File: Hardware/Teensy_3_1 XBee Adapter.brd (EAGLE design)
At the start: 27.9 x 86.4 mm, 34 parts

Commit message: Opened the board up a bit
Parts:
- removed EXT_PWR: M02PTH, SparkFun-Connectors:1X02
- added EXT_3.3V: M02PTH, SparkFun-Connectors:1X02
- JP1: value TEENSY-3.1 -> TEENSY-3.1NOSILK; device Testing:TEENSY-3.1 -> Testing:TEENSY-3.1_NOSILK
- LOGO2: value OSHW-LOGOS -> OSHW-LOGOM; device SparkFun-Aesthetics:OSHW-LOGO-S -> SparkFun-Aesthetics:OSHW-LOGO-M
- LOGO3: value SFE_LOGO_NAME_FLAME.1_INCH -> SFE_LOGO_NAME_FLAME.2_INCH; device SparkFun-Aesthetics:SFE_LOGO_NAME_FLAME_.1 -> SparkFun-Aesthetics:SFE_LOGO_NAME_FLAME_.2
- moved SJ1 53.3 mm to (5.08, 53.3)
- moved S2 49.9 mm to (10.2, 52.1)
- moved SJ3 48.4 mm to (5.08, 50.8)
- moved STANDOFF1 30.7 mm to (27.9, 81.3)
- moved STANDOFF2 30.5 mm to (5.08, 81.3)
- moved LED1 28.3 mm to (27.3, 54.6), turned to 270 degrees
- moved FID2 25.4 mm to (31.8, 1.27)
- moved FID1 24.1 mm to (1.27, 85.1)
- moved R11 24.1 mm to (24.1, 54.6), turned to 180 degrees
- moved LOGO2 16.6 mm to (21.6, 3.49)
- moved FRAME1 11.4 mm to (-17.8, -11.4)
- moved R1 10.9 mm to (15.2, 74.9)
- moved R3 10.9 mm to (12.7, 74.9)
- moved LOGO3 10.2 mm to (12.4, 14.6)
- moved STANDOFF3 9.25 mm to (16.5, 2.54)
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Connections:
- removed net EXT_PWR: EXT_PWR.2, SJ4.1, SJ5.2
- new net EXT_3.3V: EXT_3.3V.2, SJ4.1, SJ5.2
- net GND: now also EXT_3.3V.1; no longer EXT_PWR.1
- net IN: now also S2.5; no longer S2.2
- net N$140: now also S2.6; no longer S2.3
- net N$141: now also S2.3; no longer S2.6
- net OUT: now also S2.2; no longer S2.5
- net UART_RX: now also S2.1; no longer S2.4
- net UART_TX: now also S2.4; no longer S2.1
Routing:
- net EXT_3.3V: track 0.00 -> 71.8 mm, vias 0 -> 2
- net IN: track 112.8 -> 49.3 mm, vias 1 -> 2
- net EXT_PWR: track 52.3 -> 0.00 mm
- net OUT: track 101.9 -> 50.0 mm, vias 1 -> 3
- net UART_RX: track 11.7 -> 62.7 mm, vias 1 -> 2
- net UART_TX: track 21.0 -> 62.9 mm, vias 1 -> 2
- net N$43: track 17.3 -> 8.22 mm, vias 2 -> 0
- net XBEE_VDD: track 66.2 -> 57.4 mm
- net N$17: track 2.08 -> 9.50 mm
- net GND: track 56.9 -> 49.5 mm, vias 20 -> 25
- net N$19: track 2.08 -> 9.35 mm
- net A7/21: track 39.3 -> 44.1 mm
- net A5/19/SCL0: track 5.39 -> 9.72 mm
- net A9/23: track 5.39 -> 9.72 mm
- net A4/18/SDA0: track 5.39 -> 9.72 mm
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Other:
- board size 27.9 x 86.4 mm -> 33 x 86.4 mm
- board text added: "-"
- board text added: "0/RX1"
- board text added: "1/TX1"
- board text added: "11"
- board text added: "12"
- board text added: "13"
- board text added: "2"
- board text added: "3.3V"
- board text added: "3V"
- board text added: "7/RX3"
- board text added: "8/TX3"
- board text added: "A0/14"
- board text added: "A1/15"
- board text added: "A10"
- board text added: "A11"
- board text added: "A14/DAC"
- board text added: "A2/16"
- board text added: "A3/17"
- board text added: "A4/18"
- board text added: "A5/19"
- board text added: "A6/20"
- board text added: "A7/21"
- board text added: "A8/22"
- board text added: "A9/23"
- board text added: "AGND"
- board text added: "AREF"
- board text added: "DGND"
- board text added: "EXT"
- board text added: "EXT_PWR"
- board text added: "Pgm"
- board text added: "TNSY"
- board text added: "Teensy 3.1"
- board text added: "UART1"
- board text added: "VBat"
- board text added: "VIN"
- board text added: "VUSB"
- board text added: "Vin"
- board text added: "XBee"
- board text added: "~10/.."
- board text added: "~3"
- board text added: "~4"
- board text added: "~5"
- board text added: "~6"
- board text added: "~9/.."
- board text removed: "D3/D2"
- board text removed: "TNSY_PWR"
- board text removed: "UART"
- board text removed: "XBEE"

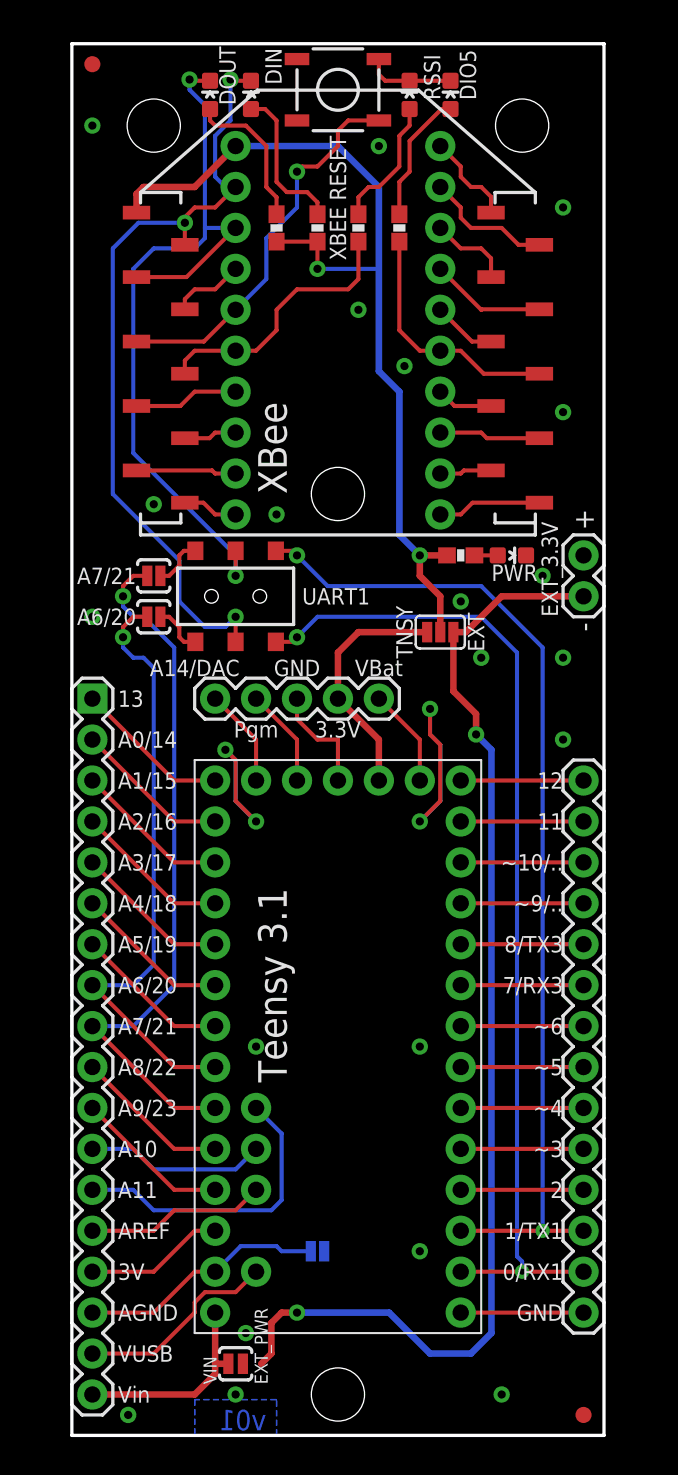
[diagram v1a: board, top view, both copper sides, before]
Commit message: Fixed silk.  Preparing for first proto
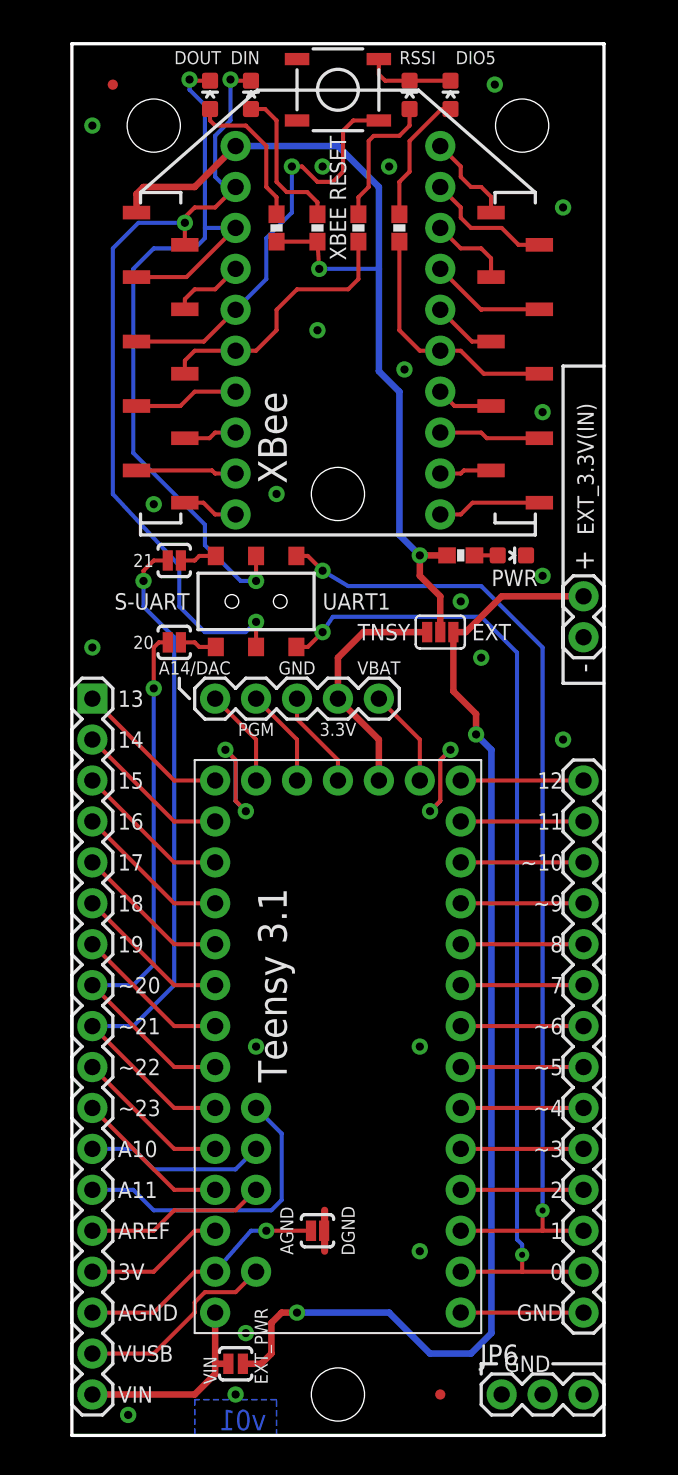
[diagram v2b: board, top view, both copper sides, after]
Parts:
- removed EXT_3.3V: M02PTH, SparkFun-Connectors:1X02
- added EXT_3.3V(IN): M02PTH, SparkFun-Connectors:1X02
- added JP6: (no value), SparkFun-Connectors:1X03
- FID1, FID2: value FIDUCIAL1X2 -> FIDUCIALUFIDUCIAL; device SparkFun-Aesthetics:FIDUCIAL-1X2 -> SparkFun-Aesthetics:MICRO-FIDUCIAL
- SJ2: device SparkFun:SJ_2S -> SparkFun-Passives:PAD-JUMPER-2-NC_BY_PASTE_YES_SILK
- moved FID2 8.98 mm to (22.9, 2.54)
- moved SJ3 2.03 mm to (6.35, 49.2)
- moved FID1 1.80 mm to (2.54, 83.8)
- moved SJ1 1.59 mm to (6.35, 54.3)
- moved S2 1.31 mm to (11.4, 51.8)
- moved SJ2 1.27 mm to (15.2, 12.7), flipped to the top, turned to 0 degrees
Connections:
- net EXT_3.3V: now also EXT_3.3V(IN).2; no longer EXT_3.3V.2
- net GND: now also EXT_3.3V(IN).1, JP6.1, JP6.2, JP6.3; no longer EXT_3.3V.1
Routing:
- net GND: track 49.5 -> 42.6 mm
- net A6/20: track 37.9 -> 34.7 mm
- net RESET: track 24.1 -> 26.2 mm
- net UART_TX: track 62.9 -> 61.3 mm
- net OUT: track 50.0 -> 51.5 mm
- net IN: track 49.3 -> 50.7 mm
- net EXT_3.3V: track 71.8 -> 72.9 mm
- net UART_RX: track 62.7 -> 61.7 mm
- net N$141: track 3.18 -> 2.29 mm
- net N$140: track 3.18 -> 2.29 mm
- net N$43: track 8.22 -> 8.77 mm
- net AGND: track 15.4 -> 15.8 mm, vias 0 -> 1
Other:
- board text added: "0"
- board text added: "1"
- board text added: "14"
- board text added: "15"
- board text added: "16"
- board text added: "17"
- board text added: "18"
- board text added: "19"
- board text added: "20"
- board text added: "21"
- board text added: "7"
- board text added: "8"
- board text added: "PGM"
- board text added: "S-UART"
- board text added: "VBAT"
- board text added: "~10"
- board text added: "~20"
- board text added: "~21"
- board text added: "~22"
- board text added: "~23"
- board text added: "~9"
- board text removed: "0/RX1"
- board text removed: "1/TX1"
- board text removed: "7/RX3"
- board text removed: "8/TX3"
- board text removed: "A0/14"
- board text removed: "A1/15"
- board text removed: "A2/16"
- board text removed: "A3/17"
- board text removed: "A4/18"
- board text removed: "A5/19"
- board text removed: "A6/20"
- board text removed: "A7/21"
- board text removed: "A8/22"
- board text removed: "A9/23"
- board text removed: "Pgm"
- board text removed: "VBat"
- board text removed: "Vin"
- board text removed: "~10/.."
- board text removed: "~9/.."

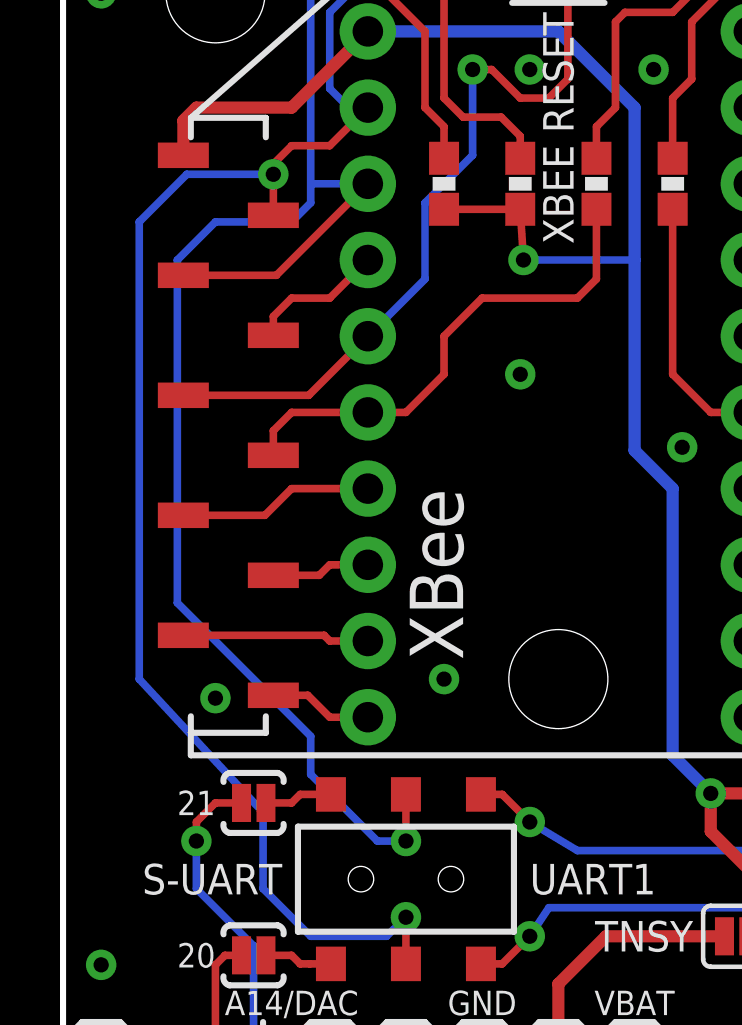
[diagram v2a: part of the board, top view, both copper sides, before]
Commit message: Fliping bottom silk labels
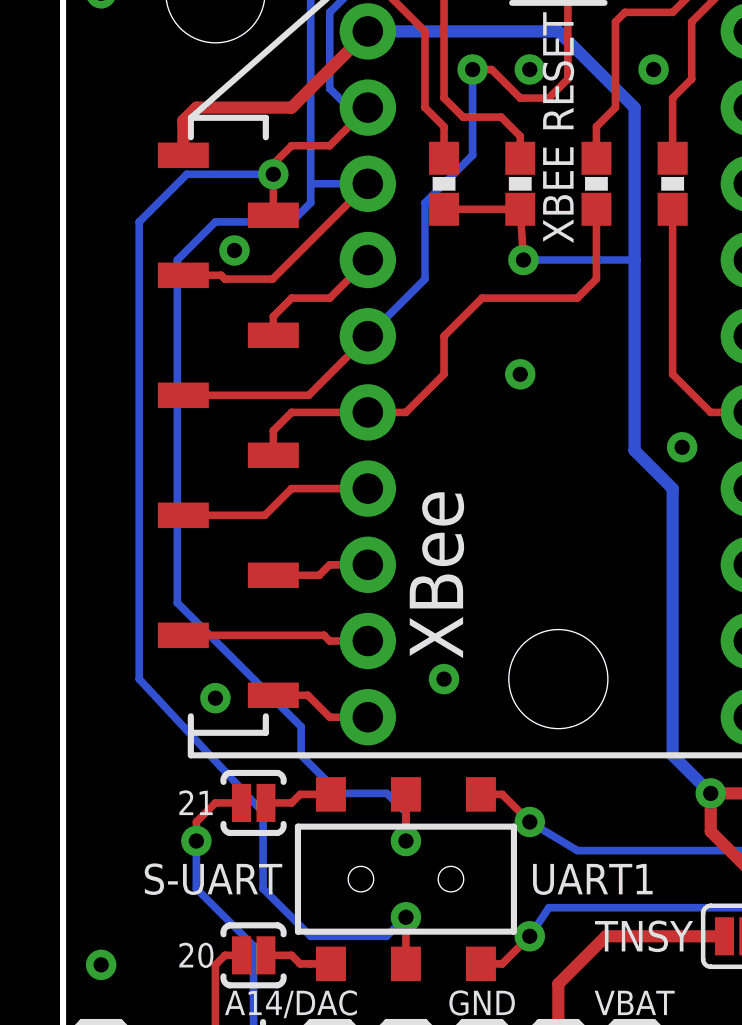
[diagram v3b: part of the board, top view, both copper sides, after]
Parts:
- moved LOGO2 0.71 mm to (22.2, 3.17), turned to 0 degrees
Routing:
- net GND: vias 25 -> 26
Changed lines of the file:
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@@
 <grid distance="0.1" unitdist="inch" unit="inch" style="lines" multiple="1" display="yes" altdistance="0.0125" altunitdist="inch" altunit="inch"/>
 <layers>
-<layer number="1" name="Top" color="4" fill="1" visible="yes" active="yes"/>
+<layer number="1" name="Top" color="4" fill="1" visible="no" active="yes"/>
 <layer number="2" name="Route2" color="1" fill="3" visible="no" active="no"/>
 <layer number="3" name="Route3" color="4" fill="3" visible="no" active="no"/>
@@
 <text x="11.43" y="64.77" size="1.016" layer="22" font="vector" ratio="15" rot="MR0" align="center-right">DIO11</text>
 <text x="11.43" y="62.23" size="1.016" layer="22" font="vector" ratio="15" rot="MR0" align="center-right">RES</text>
-<text x="11.43" y="59.69" size="1.016" layer="22" font="vector" ratio="15" rot="MR0" align="center-right">DTR</text>
-<text x="11.43" y="57.15" size="1.016" layer="22" font="vector" ratio="15" rot="MR0" align="center-right">GND</text>
+<text x="8.5725" y="59.69" size="1.016" layer="22" font="vector" ratio="15" rot="MR0" align="center-left">DTR</text>
+<text x="8.5725" y="57.15" size="1.016" layer="22" font="vector" ratio="15" rot="MR0" align="center-left">GND</text>
 <text x="21.2471" y="77.47" size="1.016" layer="22" font="vector" ratio="15" rot="MR0" align="center-left">DIO1</text>
 <text x="21.2471" y="74.93" size="1.016" layer="22" font="vector" ratio="15" rot="MR0" align="center-left">DIO2</text>
 <text x="21.2471" y="72.39" size="1.016" layer="22" font="vector" ratio="15" rot="MR0" align="center-left">DIO3</text>
-<text x="24.4221" y="69.85" size="1.016" layer="22" font="vector" ratio="15" rot="MR0" align="center-right">RTS</text>
-<text x="24.4221" y="67.31" size="1.016" layer="22" font="vector" ratio="15" rot="MR0" align="center-right">DIO5</text>
-<text x="24.4221" y="64.77" size="1.016" layer="22" font="vector" ratio="15" rot="MR0" align="center-right">RES</text>
-<text x="24.4221" y="62.23" size="1.016" layer="22" font="vector" ratio="15" rot="MR0" align="center-right">DIO9</text>
+<text x="21.2471" y="69.85" size="1.016" layer="22" font="vector" ratio="15" rot="MR0" align="center-left">RTS</text>
+<text x="21.2471" y="67.31" size="1.016" layer="22" font="vector" ratio="15" rot="MR0" align="center-left">DIO5</text>
+<text x="21.2471" y="64.77" size="1.016" layer="22" font="vector" ratio="15" rot="MR0" align="center-left">RES</text>
+<text x="21.2471" y="62.23" size="1.016" layer="22" font="vector" ratio="15" rot="MR0" align="center-left">DIO9</text>
 <text x="24.4221" y="59.69" size="1.016" layer="22" font="vector" ratio="15" rot="MR0" align="center-right">CTS</text>
 <text x="24.4221" y="57.15" size="1.016" layer="22" font="vector" ratio="15" rot="MR0" align="center-right">DIO4</text>
@@
 <element name="STANDOFF3" library="SparkFun-Electromechanical" package="STAND-OFF" value="STAND-OFF" x="16.51" y="2.54"/>
 <element name="STANDOFF4" library="SparkFun-Electromechanical" package="STAND-OFF" value="STAND-OFF" x="16.51" y="58.42"/>
-<element name="LOGO2" library="SparkFun-Aesthetics" package="OSHW-LOGO-M" value="OSHW-LOGOM" x="21.59" y="3.4925" rot="MR90"/>
+<element name="LOGO2" library="SparkFun-Aesthetics" package="OSHW-LOGO-M" value="OSHW-LOGOM" x="22.225" y="3.175" rot="MR0"/>
 <element name="LOGO3" library="SparkFun-Aesthetics" package="SFE_LOGO_NAME_FLAME_.2" value="SFE_LOGO_NAME_FLAME.2_INCH" x="12.3825" y="14.605" rot="MR90"/>
 <element name="S2" library="SparkFun" package="AYZ0202" value="SWITCH-DPDTSMD" x="11.43" y="51.7525" smashed="yes" rot="R180"/>
@@
 <contactref element="JP2" pad="8"/>
 <contactref element="LED3" pad="C"/>
-<wire x1="4.01" y1="71.88" x2="7.11" y2="71.88" width="0.254" layer="1"/>
-<wire x1="7.11" y1="71.88" x2="10.16" y2="74.93" width="0.254" layer="1"/>
+<wire x1="4.01" y1="71.88" x2="5.2725" y2="71.88" width="0.254" layer="1"/>
+<wire x1="5.2725" y1="71.88" x2="5.3975" y2="71.755" width="0.254" layer="1"/>
+<wire x1="5.3975" y1="71.755" x2="6.985" y2="71.755" width="0.254" layer="1"/>
+<wire x1="6.985" y1="71.755" x2="10.16" y2="74.93" width="0.254" layer="1"/>
 <wire x1="10.16" y1="74.93" x2="8.255" y2="74.93" width="0.254" layer="16"/>
 <wire x1="8.255" y1="74.295" x2="8.255" y2="74.93" width="0.254" layer="16"/>
@@
 <wire x1="11.43" y1="54.5775" x2="11.43" y2="53.0225" width="0.254" layer="1"/>
 <via x="11.43" y="53.0225" extent="1-16" drill="0.508"/>
-<wire x1="11.43" y1="53.0225" x2="10.4775" y2="53.0225" width="0.254" layer="16"/>
-<wire x1="10.4775" y1="53.0225" x2="8.255" y2="55.245" width="0.254" layer="16"/>
-<wire x1="8.255" y1="55.245" x2="8.255" y2="56.515" width="0.254" layer="16"/>
-<wire x1="8.255" y1="56.515" x2="3.81" y2="60.96" width="0.254" layer="16"/>
+<wire x1="11.43" y1="53.0225" x2="11.43" y2="53.975" width="0.254" layer="16"/>
+<wire x1="11.43" y1="53.975" x2="10.795" y2="54.61" width="0.254" layer="16"/>
+<wire x1="10.795" y1="54.61" x2="9.2075" y2="54.61" width="0.254" layer="16"/>
+<wire x1="9.2075" y1="54.61" x2="7.9375" y2="55.88" width="0.254" layer="16"/>
+<wire x1="7.9375" y1="55.88" x2="7.9375" y2="56.8325" width="0.254" layer="16"/>
+<wire x1="7.9375" y1="56.8325" x2="3.81" y2="60.96" width="0.254" layer="16"/>
 <wire x1="3.81" y1="60.96" x2="3.81" y2="72.39" width="0.254" layer="16"/>
 <wire x1="3.81" y1="72.39" x2="5.08" y2="73.66" width="0.254" layer="16"/>
@@
 <contactref element="JP6" pad="2"/>
 <contactref element="JP6" pad="3"/>
+<via x="5.715" y="72.7075" extent="1-16" drill="0.508"/>
 </signal>
 <signal name="DIO4">

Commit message: Completed first round of QC notes
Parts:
- removed EXT_3.3V(IN): M02PTH, SparkFun-Connectors:1X02
- removed U$2: M18_, SparkFun-Connectors:1X18
- added JP7: DNP\, SparkFun-Connectors:1X18
- added JP8: DNP, SparkFun-Connectors:1X02
- JP2, JP3: value M10NO_SILK_PTH_FEMALE -> (none)
- JP4: value M14 -> DNP
- JP5, JP6: value (none) -> DNP
- JP9: value XBEE-1B3 -> CONN-09042
- S2: value SWITCH-DPDTSMD -> DPDT; device SparkFun:AYZ0202 -> SparkFun-Electromechanical:AYZ0202
- S3: device SparkFun:TACTILE_SWITCH_SMD -> SparkFun-Electromechanical:TACTILE-SWITCH-SMD
- renumbered U$1 to JP9
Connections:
- net 13/SCK: now also JP7.18; no longer U$2.1
- net 3V: now also JP7.4; no longer U$2.15
- net A0/14: now also JP7.17; no longer U$2.2
- net A1/15: now also JP7.16; no longer U$2.3
- net A10: now also JP7.7; no longer U$2.12
- net A11: now also JP7.6; no longer U$2.13
- net A2/16: now also JP7.15; no longer U$2.4
- net A3/17: now also JP7.14; no longer U$2.5
- net A4/18/SDA0: now also JP7.13; no longer U$2.6
- net A5/19/SCL0: now also JP7.12; no longer U$2.7
- net A6/20: now also JP7.11; no longer U$2.8
- net A7/21: now also JP7.10; no longer U$2.9
- net A8/22: now also JP7.9; no longer U$2.10
- net A9/23: now also JP7.8; no longer U$2.11
- net AGND: now also JP7.3; no longer U$2.16
- net AREF: now also JP7.5; no longer U$2.14
- net EXT_3.3V: now also JP8.1; no longer EXT_3.3V(IN).2
- net GND: now also JP8.2; no longer EXT_3.3V(IN).1
- net VIN: now also JP7.1; no longer U$2.18
- net VUSB: now also JP7.2; no longer U$2.17
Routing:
- net A3/17: track 9.72 -> 2.54 mm
- net GND: track 42.6 -> 38.9 mm
- net XBEE_VDD: track 57.3 -> 59.6 mm
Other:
- board text added: "EXT_PWR (3.3V)"

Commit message: Fixed airwire, updated revision
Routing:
- net A3/17: track 2.54 -> 9.72 mm
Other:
- board text added: "v03"
- board text removed: "v01"
